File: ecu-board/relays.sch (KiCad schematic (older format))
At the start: 4 parts, among them K1 Main power relay, K2 Start motor relay

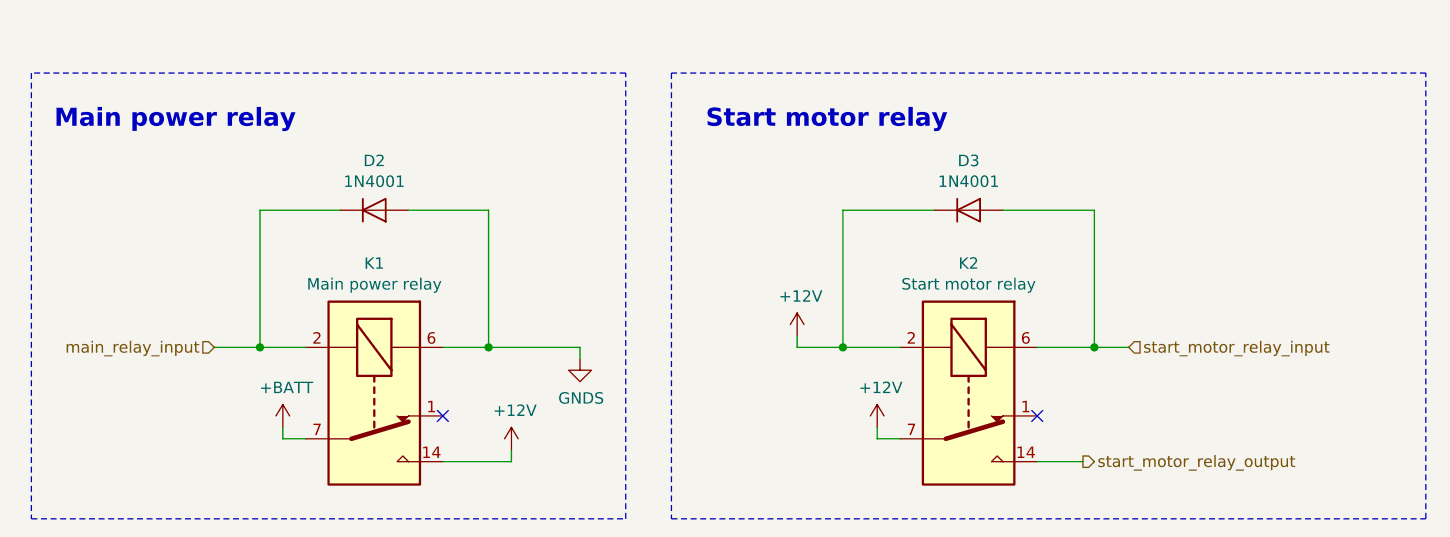
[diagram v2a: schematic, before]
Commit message: Add relay article information.
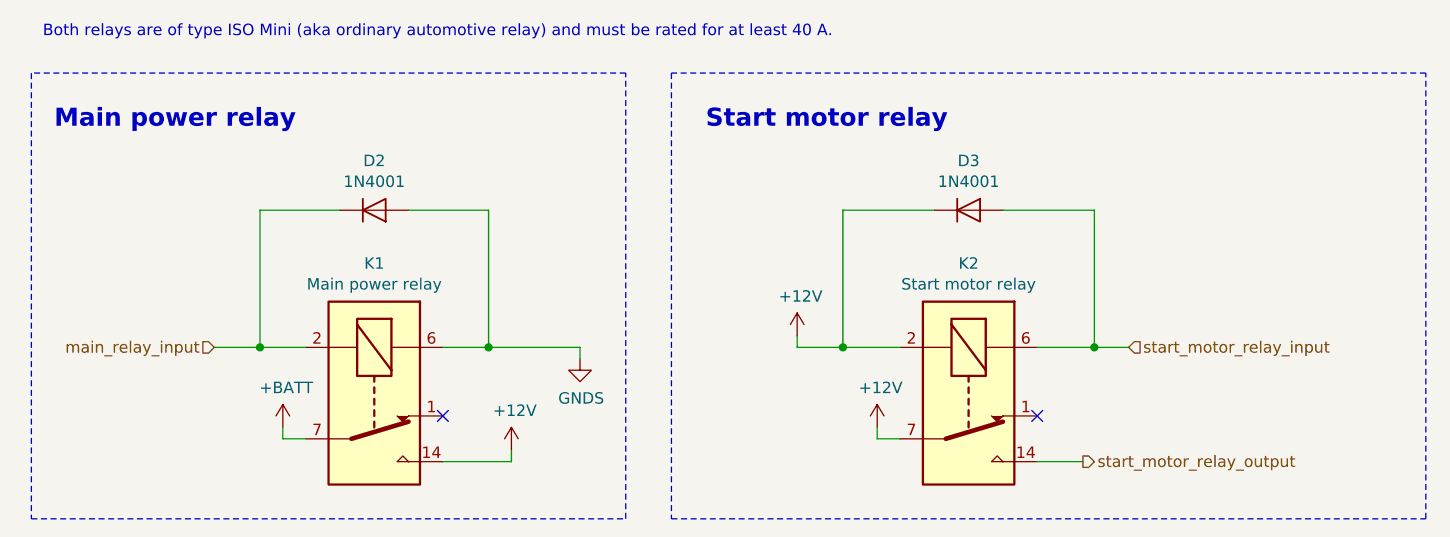
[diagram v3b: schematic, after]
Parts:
- K1, K2: Farnell 1024021 -> (none); Manufacturer (none) -> TE Connectivity; Part no. (none) -> V23333-Z0002-A041
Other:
- note added: "Both relays are of type ISO Mini (aka ordinary automotive relay) and must be rated for at least 40 A."
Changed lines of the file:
@@
 F 1 "Main power relay" V 3624 3800 50  0000 C CNN
 F 2 "" H 4550 3750 50  0001 L CNN
-F 3 "http://www.farnell.com/datasheets/1736846.pdf?_ga=2.224285851.1892952727.1549112209-881392492.1520553087" H 4100 3800 50  0001 C CNN
-F 4 "1024021" H 4100 3800 50  0001 C CNN "Farnell"
+F 3 "" H 4100 3800 50  0001 C CNN
+F 4 "TE Connectivity" H 4100 3800 50  0001 C CNN "Manufacturer"
+F 5 "V23333-Z0002-A041" H 4100 3800 50  0001 C CNN "Part no."
 	1    4100 3800
 	0    1    1    0
@@
 F 1 "Start motor relay" V 6224 3800 50  0000 C CNN
 F 2 "" H 7150 3750 50  0001 L CNN
-F 3 "http://www.farnell.com/datasheets/1736846.pdf?_ga=2.224285851.1892952727.1549112209-881392492.1520553087" H 6700 3800 50  0001 C CNN
-F 4 "1024021" H 6700 3800 50  0001 C CNN "Farnell"
+F 3 "" H 6700 3800 50  0001 C CNN
+F 4 "TE Connectivity" H 6700 3800 50  0001 C CNN "Manufacturer"
+F 5 "V23333-Z0002-A041" H 6700 3800 50  0001 C CNN "Part no."
 	1    6700 3800
 	0    1    1    0
@@
 Wire Wire Line
 	5950 3600 6150 3600
+Text Notes 2650 2250 0    50   ~ 0
+Both relays are of type ISO Mini (aka ordinary automotive relay) and must be rated for at least 40 A.
 $EndSCHEMATC

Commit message: Change diodes.
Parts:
- D2, D3: value 1N4001 -> 1N5820G; Farnell 2675791 -> (none); Manufacturer (none) -> ON Semi; Part no. (none) -> 1N5820G
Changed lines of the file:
@@
 P 4100 3000
 F 0 "D2" H 4100 2784 50  0000 C CNN
-F 1 "1N4001" H 4100 2875 50  0000 C CNN
+F 1 "1N5820G" H 4100 2875 50  0000 C CNN
 F 2 "" H 4100 3000 50  0001 C CNN
 F 3 "~" H 4100 3000 50  0001 C CNN
-F 4 "2675791" H 4100 3000 50  0001 C CNN "Farnell"
+F 4 "ON Semi" H 4100 3000 50  0001 C CNN "Manufacturer"
+F 5 "1N5820G" H 4100 3000 50  0001 C CNN "Part no."
 	1    4100 3000
 	1    0    0    1
@@
 P 6700 3000
 F 0 "D3" H 6700 3216 50  0000 C CNN
-F 1 "1N4001" H 6700 3125 50  0000 C CNN
+F 1 "1N5820G" H 6700 3125 50  0000 C CNN
 F 2 "" H 6700 3000 50  0001 C CNN
 F 3 "~" H 6700 3000 50  0001 C CNN
-F 4 "2675791" H 6700 3000 50  0001 C CNN "Farnell"
+F 4 "ON Semi" H 6700 3000 50  0001 C CNN "Manufacturer"
+F 5 "1N5820G" H 6700 3000 50  0001 C CNN "Part no."
 	1    6700 3000
 	1    0    0    -1

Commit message: Assign diode footprints.
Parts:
- D2, D3: footprint (none) -> Diodes_THT:D_A-405_P10.16mm_Horizontal
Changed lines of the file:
@@
 F 0 "D2" H 4100 2784 50  0000 C CNN
 F 1 "1N5820G" H 4100 2875 50  0000 C CNN
-F 2 "" H 4100 3000 50  0001 C CNN
+F 2 "Diodes_THT:D_A-405_P10.16mm_Horizontal" H 4100 3000 50  0001 C CNN
 F 3 "~" H 4100 3000 50  0001 C CNN
 F 4 "ON Semi" H 4100 3000 50  0001 C CNN "Manufacturer"
@@
 F 0 "D3" H 6700 3216 50  0000 C CNN
 F 1 "1N5820G" H 6700 3125 50  0000 C CNN
-F 2 "" H 6700 3000 50  0001 C CNN
+F 2 "Diodes_THT:D_A-405_P10.16mm_Horizontal" H 6700 3000 50  0001 C CNN
 F 3 "~" H 6700 3000 50  0001 C CNN
 F 4 "ON Semi" H 6700 3000 50  0001 C CNN "Manufacturer"

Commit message: Assign relay footprints.
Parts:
- K1, K2: footprint (none) -> ecu-board-footprints:TE_2-1904045-4
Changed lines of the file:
@@
 F 0 "K1" V 3533 3800 50  0000 C CNN
 F 1 "Main power relay" V 3624 3800 50  0000 C CNN
-F 2 "" H 4550 3750 50  0001 L CNN
+F 2 "ecu-board-footprints:TE_2-1904045-4" H 4550 3750 50  0001 L CNN
 F 3 "" H 4100 3800 50  0001 C CNN
 F 4 "TE Connectivity" H 4100 3800 50  0001 C CNN "Manufacturer"
@@
 F 0 "K2" V 6133 3800 50  0000 C CNN
 F 1 "Start motor relay" V 6224 3800 50  0000 C CNN
-F 2 "" H 7150 3750 50  0001 L CNN
+F 2 "ecu-board-footprints:TE_2-1904045-4" H 7150 3750 50  0001 L CNN
 F 3 "" H 6700 3800 50  0001 C CNN
 F 4 "TE Connectivity" H 6700 3800 50  0001 C CNN "Manufacturer"

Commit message: Ignore lib cache files.
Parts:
- K1, K2: symbol Relay:DIPxx-1Cxx-51x -> ecu-board:Mini_ISO_relay
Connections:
- net +12V: now also K1.87, K2.30, K2.86; no longer K1.14, K2.2, K2.7, K2.8
- net +BATT: now also K1.30; no longer K1.7, K1.8
- net GNDS: now also K1.85; no longer K1.6
- net main_relay_input: now also K1.86; no longer K1.2
- net start_motor_relay_input: now also K2.85; no longer K2.6
- net start_motor_relay_output: now also K2.87; no longer K2.14
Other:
- moved on the sheet: D2, D3, K1, K2
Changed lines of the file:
@@
 $EndDescr
 $Comp
-L Relay:DIPxx-1Cxx-51x K1
-U 1 1 5C6BEAC6
-P 4100 3800
-F 0 "K1" V 3533 3800 50  0000 C CNN
-F 1 "Main power relay" V 3624 3800 50  0000 C CNN
-F 2 "ecu-board-footprints:TE_2-1904045-4" H 4550 3750 50  0001 L CNN
-F 3 "" H 4100 3800 50  0001 C CNN
-F 4 "TE Connectivity" H 4100 3800 50  0001 C CNN "Manufacturer"
-F 5 "V23333-Z0002-A041" H 4100 3800 50  0001 C CNN "Part no."
-	1    4100 3800
-	0    1    1    0
-$EndComp
-$Comp
-L Relay:DIPxx-1Cxx-51x K2
+L ecu-board:Mini_ISO_relay K2
 U 1 1 5C6BEC94
-P 6700 3800
-F 0 "K2" V 6133 3800 50  0000 C CNN
-F 1 "Start motor relay" V 6224 3800 50  0000 C CNN
-F 2 "ecu-board-footprints:TE_2-1904045-4" H 7150 3750 50  0001 L CNN
-F 3 "" H 6700 3800 50  0001 C CNN
-F 4 "TE Connectivity" H 6700 3800 50  0001 C CNN "Manufacturer"
-F 5 "V23333-Z0002-A041" H 6700 3800 50  0001 C CNN "Part no."
-	1    6700 3800
-	0    1    1    0
+P 7000 3700
+F 0 "K2" H 6850 4150 50  0000 C CNN
+F 1 "Start motor relay" H 7000 3250 50  0000 C CNN
+F 2 "ecu-board-footprints:TE_2-1904045-4" H 7450 3650 50  0001 L CNN
+F 3 "" H 7000 3700 50  0001 C CNN
+F 4 "TE Connectivity" H 7000 3700 50  0001 C CNN "Manufacturer"
+F 5 "V23333-Z0002-A041" H 7000 3700 50  0001 C CNN "Part no."
+	1    7000 3700
+	1    0    0    -1
 $EndComp
 $Comp
 L Device:D D2
 U 1 1 5C6BEE87
-P 4100 3000
-F 0 "D2" H 4100 2784 50  0000 C CNN
-F 1 "1N5820G" H 4100 2875 50  0000 C CNN
-F 2 "Diodes_THT:D_A-405_P10.16mm_Horizontal" H 4100 3000 50  0001 C CNN
-F 3 "~" H 4100 3000 50  0001 C CNN
-F 4 "ON Semi" H 4100 3000 50  0001 C CNN "Manufacturer"
-F 5 "1N5820G" H 4100 3000 50  0001 C CNN "Part no."
-	1    4100 3000
-	1    0    0    1
+P 3800 3000
+F 0 "D2" H 3800 3200 50  0000 C CNN
+F 1 "1N5820G" H 3800 3100 50  0000 C CNN
+F 2 "Diodes_THT:D_A-405_P10.16mm_Horizontal" H 3800 3000 50  0001 C CNN
+F 3 "~" H 3800 3000 50  0001 C CNN
+F 4 "ON Semi" H 3800 3000 50  0001 C CNN "Manufacturer"
+F 5 "1N5820G" H 3800 3000 50  0001 C CNN "Part no."
+	1    3800 3000
+	-1   0    0    -1
 $EndComp
 $Comp
 L Device:D D3
 U 1 1 5C6BEF1F
-P 6700 3000
-F 0 "D3" H 6700 3216 50  0000 C CNN
-F 1 "1N5820G" H 6700 3125 50  0000 C CNN
-F 2 "Diodes_THT:D_A-405_P10.16mm_Horizontal" H 6700 3000 50  0001 C CNN
-F 3 "~" H 6700 3000 50  0001 C CNN
-F 4 "ON Semi" H 6700 3000 50  0001 C CNN "Manufacturer"
-F 5 "1N5820G" H 6700 3000 50  0001 C CNN "Part no."
-	1    6700 3000
-	1    0    0    -1
+P 7000 2900
+F 0 "D3" H 7000 2700 50  0000 C CNN
+F 1 "1N5820G" H 7000 2800 50  0000 C CNN
+F 2 "Diodes_THT:D_A-405_P10.16mm_Horizontal" H 7000 2900 50  0001 C CNN
+F 3 "~" H 7000 2900 50  0001 C CNN
+F 4 "ON Semi" H 7000 2900 50  0001 C CNN "Manufacturer"
+F 5 "1N5820G" H 7000 2900 50  0001 C CNN "Part no."
+	1    7000 2900
+	-1   0    0    1
 $EndComp
 Wire Wire Line
-	3950 3000 3600 3000
+	3650 3000 3350 3000
 Wire Wire Line
-	3600 3000 3600 3600
+	3950 3000 4250 3000
 Wire Wire Line
-	3600 3600 3800 3600
-Wire Wire Line
-	4250 3000 4600 3000
-Wire Wire Line
-	4600 3000 4600 3600
-Wire Wire Line
-	4600 3600 4400 3600
-Wire Wire Line
-	6550 3000 6150 3000
-Wire Wire Line
-	6150 3000 6150 3600
-Wire Wire Line
-	6150 3600 6400 3600
-Wire Wire Line
-	7250 3000 7250 3600
-Wire Wire Line
-	7250 3600 7000 3600
+	6850 2900 6550 2900
 $Comp
 L power:+BATT #PWR026
 U 1 1 5C6C2CF3
-P 3700 3950
-F 0 "#PWR026" H 3700 3800 50  0001 C CNN
-F 1 "+BATT" H 3715 4123 50  0000 C CNN
-F 2 "" H 3700 3950 50  0001 C CNN
-F 3 "" H 3700 3950 50  0001 C CNN
-	1    3700 3950
+P 3350 3850
+F 0 "#PWR026" H 3350 3700 50  0001 C CNN
+F 1 "+BATT" H 3365 4023 50  0000 C CNN
+F 2 "" H 3350 3850 50  0001 C CNN
+F 3 "" H 3350 3850 50  0001 C CNN
+	1    3350 3850
 	1    0    0    -1
 $EndComp
-Wire Wire Line
-	3700 3950 3700 4000
-Wire Wire Line
-	3700 4000 3800 4000
-NoConn ~ 7000 3900
-NoConn ~ 4400 3900
+NoConn ~ 7400 3800
 $Comp
 L power:+12V #PWR027
 U 1 1 5C6C5187
-P 4700 4050
-F 0 "#PWR027" H 4700 3900 50  0001 C CNN
-F 1 "+12V" H 4715 4223 50  0000 C CNN
-F 2 "" H 4700 4050 50  0001 C CNN
-F 3 "" H 4700 4050 50  0001 C CNN
-	1    4700 4050
+P 4400 3950
+F 0 "#PWR027" H 4400 3800 50  0001 C CNN
+F 1 "+12V" H 4415 4123 50  0000 C CNN
+F 2 "" H 4400 3950 50  0001 C CNN
+F 3 "" H 4400 3950 50  0001 C CNN
+	1    4400 3950
 	1    0    0    -1
 $EndComp
-Wire Wire Line
-	4700 4050 4700 4100
-Wire Wire Line
-	4700 4100 4400 4100
-Text HLabel 7200 4100 2    50   Output ~ 0
+Text HLabel 7500 4000 2    50   Output ~ 0
 start_motor_relay_output
-Wire Wire Line
-	7200 4100 7000 4100
 $Comp
 L power:+12V #PWR029
 U 1 1 5C6C6B16
-P 6300 3950
-F 0 "#PWR029" H 6300 3800 50  0001 C CNN
-F 1 "+12V" H 6315 4123 50  0000 C CNN
-F 2 "" H 6300 3950 50  0001 C CNN
-F 3 "" H 6300 3950 50  0001 C CNN
-	1    6300 3950
+P 6550 3850
+F 0 "#PWR029" H 6550 3700 50  0001 C CNN
+F 1 "+12V" H 6565 4023 50  0000 C CNN
+F 2 "" H 6550 3850 50  0001 C CNN
+F 3 "" H 6550 3850 50  0001 C CNN
+	1    6550 3850
 	1    0    0    -1
 $EndComp
-Wire Wire Line
-	6300 3950 6300 4000
-Wire Wire Line
-	6300 4000 6400 4000
-Text HLabel 3400 3600 0    50   Input ~ 0
+Text HLabel 4400 3500 2    50   Input ~ 0
 main_relay_input
-Wire Wire Line
-	3400 3600 3600 3600
-Connection ~ 3600 3600
 $Comp
 L power:GNDS #PWR028
 U 1 1 5C6C86CC
-P 5000 3650
-F 0 "#PWR028" H 5000 3400 50  0001 C CNN
-F 1 "GNDS" H 5005 3477 50  0000 C CNN
-F 2 "" H 5000 3650 50  0001 C CNN
-F 3 "" H 5000 3650 50  0001 C CNN
-	1    5000 3650
+P 3100 3550
+F 0 "#PWR028" H 3100 3300 50  0001 C CNN
+F 1 "GNDS" H 3105 3377 50  0000 C CNN
+F 2 "" H 3100 3550 50  0001 C CNN
+F 3 "" H 3100 3550 50  0001 C CNN
+	1    3100 3550
 	1    0    0    -1
 $EndComp
+Text HLabel 6500 3500 0    50   Input ~ 0
+start_motor_relay_input
 Wire Wire Line
-	5000 3650 5000 3600
-Wire Wire Line
-	5000 3600 4600 3600
-Connection ~ 4600 3600
-Text HLabel 7400 3600 2    50   Input ~ 0
-start_motor_relay_input
-Connection ~ 6150 3600
-Wire Wire Line
-	7400 3600 7250 3600
-Connection ~ 7250 3600
-Wire Wire Line
-	6850 3000 7250 3000
+	7150 2900 7450 2900
 Text Notes 2700 2650 0    79   ~ 16
 Main power relay
@@
 L power:+12V #PWR049
 U 1 1 5CE305A3
-P 5950 3550
-F 0 "#PWR049" H 5950 3400 50  0001 C CNN
-F 1 "+12V" H 5965 3723 50  0000 C CNN
-F 2 "" H 5950 3550 50  0001 C CNN
-F 3 "" H 5950 3550 50  0001 C CNN
-	1    5950 3550
+P 7700 3450
+F 0 "#PWR049" H 7700 3300 50  0001 C CNN
+F 1 "+12V" H 7715 3623 50  0000 C CNN
+F 2 "" H 7700 3450 50  0001 C CNN
+F 3 "" H 7700 3450 50  0001 C CNN
+	1    7700 3450
+	1    0    0    -1
+$EndComp
+Text Notes 2650 2250 0    50   ~ 0
+Both relays are of type ISO Mini (aka ordinary automotive relay) and must be rated for at least 40 A.
+$Comp
+L ecu-board:Mini_ISO_relay K1
+U 1 1 5C6BEAC6
+P 3800 3700
+F 0 "K1" H 3650 4150 50  0000 C CNN
+F 1 "Main power relay" H 3800 3250 50  0000 C CNN
+F 2 "ecu-board-footprints:TE_2-1904045-4" H 4250 3650 50  0001 L CNN
+F 3 "" H 3800 3700 50  0001 C CNN
+F 4 "TE Connectivity" H 3800 3700 50  0001 C CNN "Manufacturer"
+F 5 "V23333-Z0002-A041" H 3800 3700 50  0001 C CNN "Part no."
+	1    3800 3700
 	1    0    0    -1
 $EndComp
 Wire Wire Line
-	5950 3600 5950 3550
+	3350 3500 3350 3000
+Connection ~ 3350 3500
 Wire Wire Line
-	5950 3600 6150 3600
-Text Notes 2650 2250 0    50   ~ 0
-Both relays are of type ISO Mini (aka ordinary automotive relay) and must be rated for at least 40 A.
+	3350 3500 3400 3500
+Wire Wire Line
+	4200 3500 4250 3500
+Wire Wire Line
+	4250 3500 4250 3000
+NoConn ~ 4200 3800
+Wire Wire Line
+	4400 3950 4400 4000
+Wire Wire Line
+	4400 4000 4200 4000
+Wire Wire Line
+	3350 3900 3350 3850
+Wire Wire Line
+	3350 3900 3400 3900
+Wire Wire Line
+	3100 3550 3100 3500
+Wire Wire Line
+	3100 3500 3350 3500
+Wire Wire Line
+	4400 3500 4250 3500
+Connection ~ 4250 3500
+Wire Wire Line
+	6600 3500 6550 3500
+Wire Wire Line
+	6550 3500 6550 2900
+Connection ~ 6550 3500
+Wire Wire Line
+	6550 3500 6500 3500
+Wire Wire Line
+	7450 3500 7400 3500
+Wire Wire Line
+	7450 2900 7450 3500
+Wire Wire Line
+	7450 3500 7700 3500
+Wire Wire Line
+	7700 3500 7700 3450
+Connection ~ 7450 3500
+Wire Wire Line
+	7400 4000 7500 4000
+Wire Wire Line
+	6600 3900 6550 3900
+Wire Wire Line
+	6550 3900 6550 3850
 $EndSCHEMATC
